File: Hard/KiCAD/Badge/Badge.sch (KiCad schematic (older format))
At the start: 0 parts

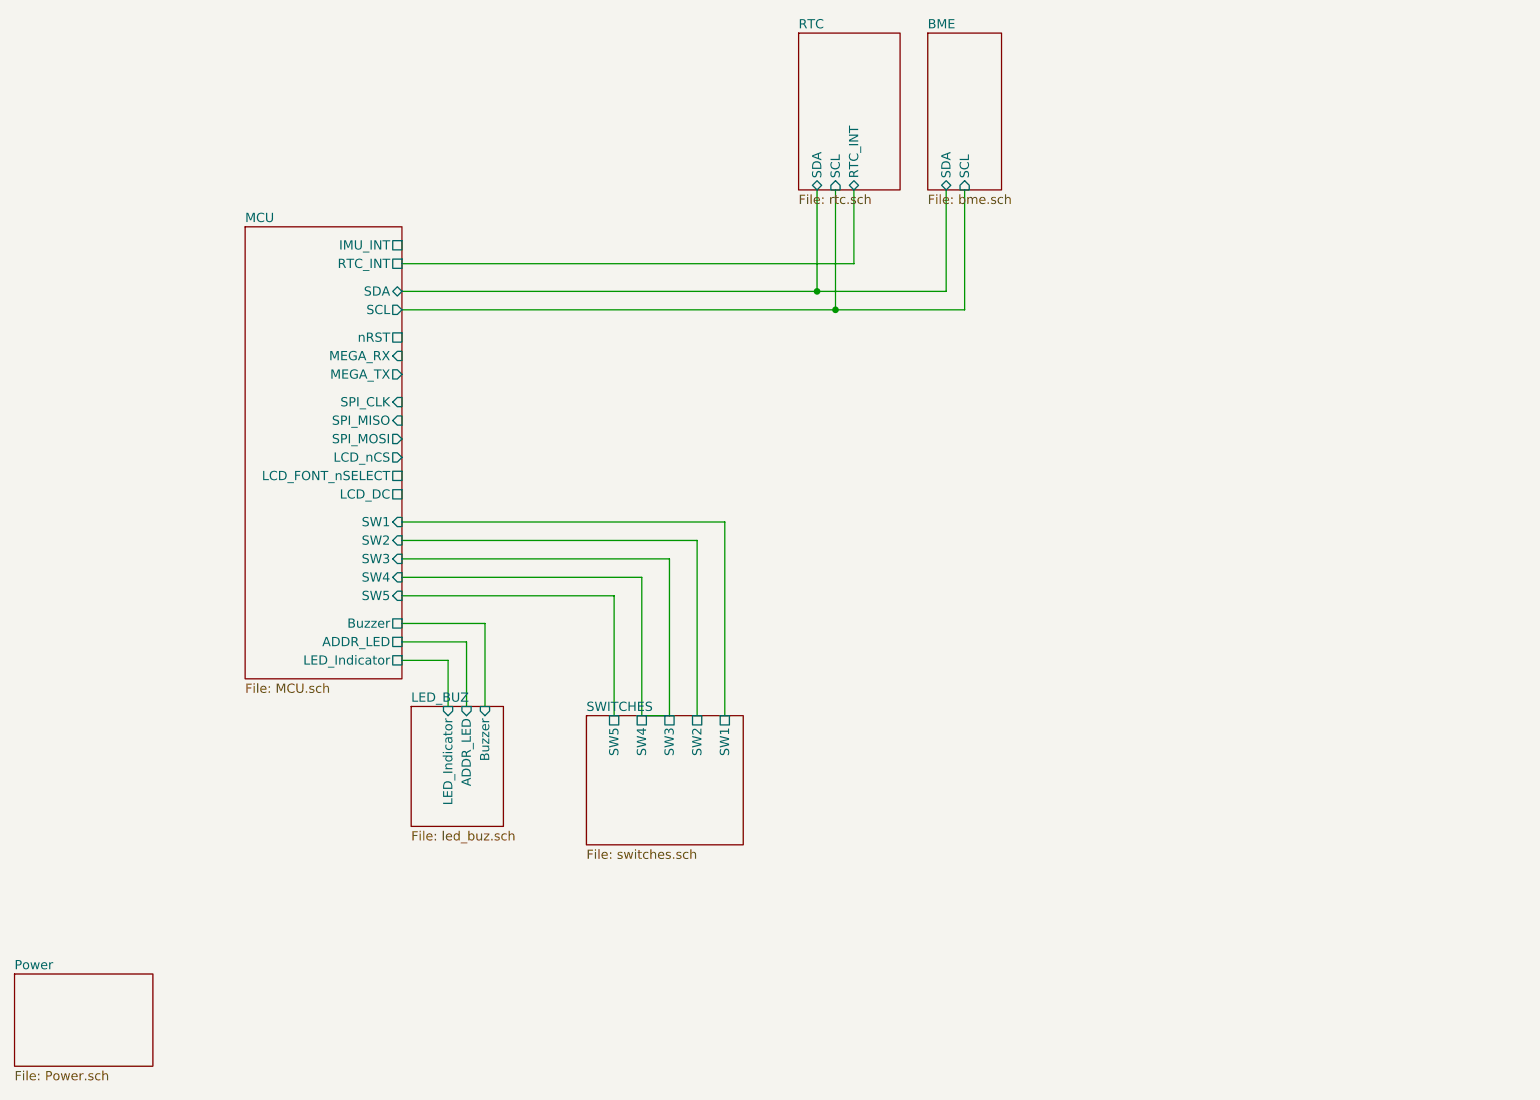
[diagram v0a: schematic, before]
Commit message: Added proposal sch for power sw
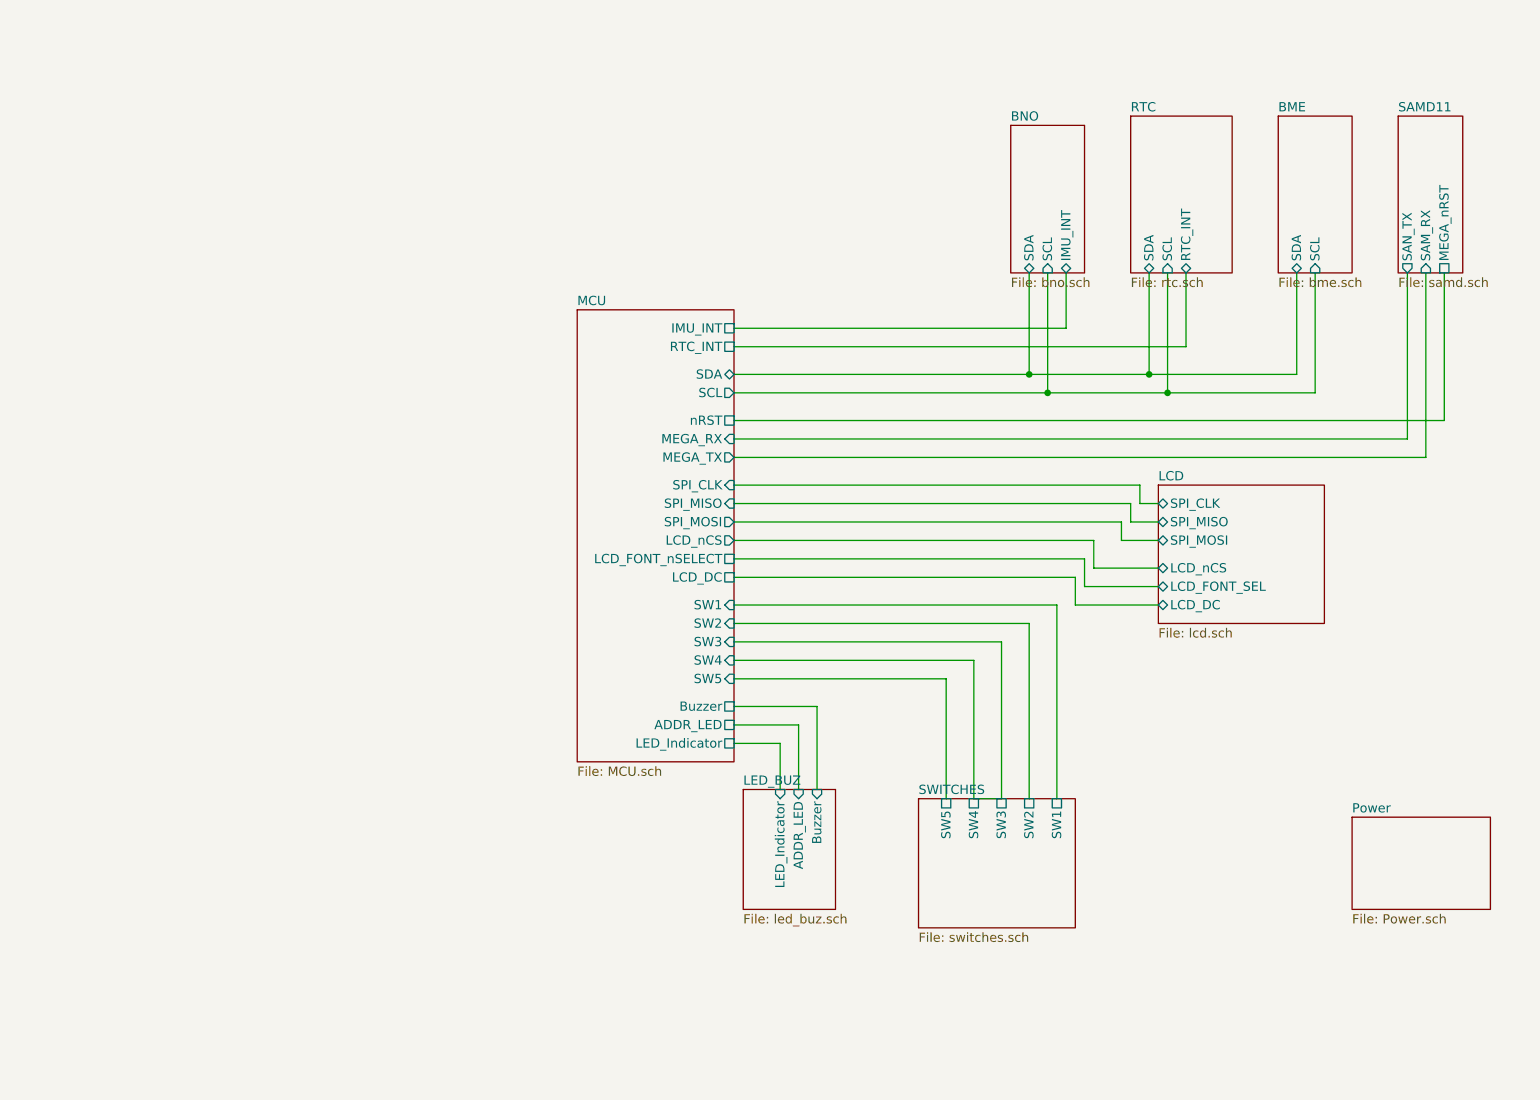
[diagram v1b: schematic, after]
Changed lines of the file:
@@
 $Descr A4 11693 8268
 encoding utf-8
-Sheet 1 7
+Sheet 1 10
 Title ""
 Date "2020-04-01"
@@
 $EndDescr
 $Sheet
-S 1950 2250 850  2450
+S 3750 2700 850  2450
 U 5E84CAB8
 F0 "MCU" 50
 F1 "MCU.sch" 50
-F2 "SDA" B R 2800 2600 50
-F3 "SCL" O R 2800 2700 50
-F4 "nRST" U R 2800 2850 50
-F5 "LED_Indicator" U R 2800 4600 50
-F6 "Buzzer" U R 2800 4400 50
-F7 "LCD_DC" U R 2800 3700 50
-F8 "SPI_MOSI" O R 2800 3400 50
-F9 "SPI_MISO" I R 2800 3300 50
-F10 "SPI_CLK" I R 2800 3200 50
-F11 "IMU_INT" U R 2800 2350 50
-F12 "RTC_INT" U R 2800 2450 50
-F13 "LCD_FONT_nSELECT" U R 2800 3600 50
-F14 "ADDR_LED" U R 2800 4500 50
-F15 "MEGA_RX" I R 2800 2950 50
-F16 "MEGA_TX" O R 2800 3050 50
-F17 "LCD_nCS" O R 2800 3500 50
-F18 "SW1" I R 2800 3850 50
-F19 "SW2" I R 2800 3950 50
-F20 "SW3" I R 2800 4050 50
-F21 "SW4" I R 2800 4150 50
-F22 "SW5" I R 2800 4250 50
-$EndSheet
-$Sheet
-S 700  6300 750  500
+F2 "SDA" B R 4600 3050 50
+F3 "SCL" O R 4600 3150 50
+F4 "nRST" U R 4600 3300 50
+F5 "LED_Indicator" U R 4600 5050 50
+F6 "Buzzer" U R 4600 4850 50
+F7 "LCD_DC" U R 4600 4150 50
+F8 "SPI_MOSI" O R 4600 3850 50
+F9 "SPI_MISO" I R 4600 3750 50
+F10 "SPI_CLK" I R 4600 3650 50
+F11 "IMU_INT" U R 4600 2800 50
+F12 "RTC_INT" U R 4600 2900 50
+F13 "LCD_FONT_nSELECT" U R 4600 4050 50
+F14 "ADDR_LED" U R 4600 4950 50
+F15 "MEGA_RX" I R 4600 3400 50
+F16 "MEGA_TX" O R 4600 3500 50
+F17 "LCD_nCS" O R 4600 3950 50
+F18 "SW1" I R 4600 4300 50
+F19 "SW2" I R 4600 4400 50
+F20 "SW3" I R 4600 4500 50
+F21 "SW4" I R 4600 4600 50
+F22 "SW5" I R 4600 4700 50
+$EndSheet
+$Sheet
+S 7950 5450 750  500
 U 5E8D6AA0
 F0 "Power" 50
@@
 $EndSheet
 $Sheet
-S 2850 4850 500  650
+S 4650 5300 500  650
 U 5E9790C2
 F0 "LED_BUZ" 50
 F1 "led_buz.sch" 50
-F2 "ADDR_LED" I T 3150 4850 50
-F3 "LED_Indicator" I T 3050 4850 50
-F4 "Buzzer" I T 3250 4850 50
-$EndSheet
-Wire Wire Line
-	3250 4850 3250 4400
-Wire Wire Line
-	3250 4400 2800 4400
-Wire Wire Line
-	2800 4500 3150 4500
-Wire Wire Line
-	3150 4500 3150 4850
-Wire Wire Line
-	3050 4850 3050 4600
-Wire Wire Line
-	3050 4600 2800 4600
-$Sheet
-S 3800 4900 850  700
+F2 "ADDR_LED" I T 4950 5300 50
+F3 "LED_Indicator" I T 4850 5300 50
+F4 "Buzzer" I T 5050 5300 50
+$EndSheet
+Wire Wire Line
+	5050 5300 5050 4850
+Wire Wire Line
+	5050 4850 4600 4850
+Wire Wire Line
+	4600 4950 4950 4950
+Wire Wire Line
+	4950 4950 4950 5300
+Wire Wire Line
+	4850 5300 4850 5050
+Wire Wire Line
+	4850 5050 4600 5050
+$Sheet
+S 5600 5350 850  700
 U 5EA1C67E
 F0 "SWITCHES" 50
 F1 "switches.sch" 50
-F2 "SW1" U T 4550 4900 50
-F3 "SW2" U T 4400 4900 50
-F4 "SW3" U T 4250 4900 50
-F5 "SW4" U T 4100 4900 50
-F6 "SW5" U T 3950 4900 50
-$EndSheet
-Wire Wire Line
-	3950 4900 3950 4250
-Wire Wire Line
-	3950 4250 2800 4250
-Wire Wire Line
-	2800 4150 4100 4150
-Wire Wire Line
-	4100 4150 4100 4900
-Wire Wire Line
-	4100 4900 4250 4900
-Wire Wire Line
-	4250 4900 4250 4050
-Wire Wire Line
-	4250 4050 2800 4050
-Wire Wire Line
-	2800 3950 4400 3950
-Wire Wire Line
-	4400 3950 4400 4900
-Wire Wire Line
-	4550 4900 4550 3850
-Wire Wire Line
-	4550 3850 2800 3850
-$Sheet
-S 5650 1200 400  850
+F2 "SW1" U T 6350 5350 50
+F3 "SW2" U T 6200 5350 50
+F4 "SW3" U T 6050 5350 50
+F5 "SW4" U T 5900 5350 50
+F6 "SW5" U T 5750 5350 50
+$EndSheet
+Wire Wire Line
+	5750 5350 5750 4700
+Wire Wire Line
+	5750 4700 4600 4700
+Wire Wire Line
+	4600 4600 5900 4600
+Wire Wire Line
+	5900 4600 5900 5350
+Wire Wire Line
+	5900 5350 6050 5350
+Wire Wire Line
+	6050 5350 6050 4500
+Wire Wire Line
+	6050 4500 4600 4500
+Wire Wire Line
+	4600 4400 6200 4400
+Wire Wire Line
+	6200 4400 6200 5350
+Wire Wire Line
+	6350 5350 6350 4300
+Wire Wire Line
+	6350 4300 4600 4300
+$Sheet
+S 7550 1650 400  850
 U 5EA62D22
 F0 "BME" 50
 F1 "bme.sch" 50
-F2 "SDA" B B 5750 2050 50
-F3 "SCL" I B 5850 2050 50
-$EndSheet
-Wire Wire Line
-	2800 2600 5050 2600
-Wire Wire Line
-	5750 2600 5750 2050
-Wire Wire Line
-	2800 2700 5150 2700
-Wire Wire Line
-	5850 2700 5850 2050
-$Sheet
-S 4950 1200 550  850
+F2 "SDA" B B 7650 2500 50
+F3 "SCL" I B 7750 2500 50
+$EndSheet
+Wire Wire Line
+	4600 3050 6200 3050
+Wire Wire Line
+	7650 3050 7650 2500
+Wire Wire Line
+	4600 3150 6300 3150
+Wire Wire Line
+	7750 3150 7750 2500
+$Sheet
+S 6750 1650 550  850
 U 5EA69527
 F0 "RTC" 50
 F1 "rtc.sch" 50
-F2 "SDA" B B 5050 2050 50
-F3 "SCL" I B 5150 2050 50
-F4 "RTC_INT" T B 5250 2050 50
-$EndSheet
-Wire Wire Line
-	5050 2050 5050 2600
-Connection ~ 5050 2600
-Wire Wire Line
-	5050 2600 5750 2600
-Wire Wire Line
-	5150 2050 5150 2700
-Connection ~ 5150 2700
-Wire Wire Line
-	5150 2700 5850 2700
-Wire Wire Line
-	2800 2450 5250 2450
-Wire Wire Line
-	5250 2450 5250 2050
+F2 "SDA" B B 6850 2500 50
+F3 "SCL" I B 6950 2500 50
+F4 "RTC_INT" T B 7050 2500 50
+$EndSheet
+Wire Wire Line
+	6850 2500 6850 3050
+Connection ~ 6850 3050
+Wire Wire Line
+	6850 3050 7650 3050
+Wire Wire Line
+	6950 2500 6950 3150
+Connection ~ 6950 3150
+Wire Wire Line
+	6950 3150 7750 3150
+Wire Wire Line
+	4600 2900 7050 2900
+Wire Wire Line
+	7050 2900 7050 2500
+$Sheet
+S 6100 1700 400  800
+U 5E89AB9A
+F0 "BNO" 50
+F1 "bno.sch" 50
+F2 "IMU_INT" T B 6400 2500 50
+F3 "SDA" B B 6200 2500 50
+F4 "SCL" I B 6300 2500 50
+$EndSheet
+Wire Wire Line
+	6200 2500 6200 3050
+Connection ~ 6200 3050
+Wire Wire Line
+	6200 3050 6850 3050
+Wire Wire Line
+	6300 2500 6300 3150
+Connection ~ 6300 3150
+Wire Wire Line
+	6300 3150 6950 3150
+Wire Wire Line
+	6400 2500 6400 2800
+Wire Wire Line
+	6400 2800 4600 2800
+$Sheet
+S 8200 1650 350  850
+U 5E8D2E3A
+F0 "SAMD11" 50
+F1 "samd.sch" 50
+F2 "SAN_TX" O B 8250 2500 50
+F3 "SAM_RX" I B 8350 2500 50
+F4 "MEGA_nRST" U B 8450 2500 50
+$EndSheet
+Wire Wire Line
+	4600 3300 8450 3300
+Wire Wire Line
+	8450 3300 8450 2500
+Wire Wire Line
+	4600 3400 8250 3400
+Wire Wire Line
+	8250 3400 8250 2500
+Wire Wire Line
+	4600 3500 8350 3500
+Wire Wire Line
+	8350 3500 8350 2500
+$Sheet
+S 6900 3650 900  750
+U 5E93C950
+F0 "LCD" 50
+F1 "lcd.sch" 50
+F2 "SPI_MISO" B L 6900 3850 50
+F3 "LCD_FONT_SEL" B L 6900 4200 50
+F4 "SPI_CLK" B L 6900 3750 50
+F5 "SPI_MOSI" B L 6900 3950 50
+F6 "LCD_DC" B L 6900 4300 50
+F7 "LCD_nCS" B L 6900 4100 50
+$EndSheet
+Wire Wire Line
+	4600 3650 6800 3650
+Wire Wire Line
+	6800 3650 6800 3750
+Wire Wire Line
+	6800 3750 6900 3750
+Wire Wire Line
+	6900 3850 6750 3850
+Wire Wire Line
+	6750 3850 6750 3750
+Wire Wire Line
+	6750 3750 4600 3750
+Wire Wire Line
+	4600 3850 6700 3850
+Wire Wire Line
+	6700 3850 6700 3950
+Wire Wire Line
+	6700 3950 6900 3950
+Wire Wire Line
+	6900 4100 6550 4100
+Wire Wire Line
+	6550 4100 6550 3950
+Wire Wire Line
+	6550 3950 4600 3950
+Wire Wire Line
+	4600 4050 6500 4050
+Wire Wire Line
+	6500 4050 6500 4200
+Wire Wire Line
+	6500 4200 6900 4200
+Wire Wire Line
+	6900 4300 6450 4300
+Wire Wire Line
+	6450 4300 6450 4150
+Wire Wire Line
+	6450 4150 4600 4150
 $EndSCHEMATC
